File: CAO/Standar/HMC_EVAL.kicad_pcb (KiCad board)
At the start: 2 copper layers, 71 x 83 mm, 57 parts, among them J1 Conn_01x03, J2 Conn_01x03, Q1 IRF7319IPBF, SW1 SW_Push, U1 OPA2209, U2 HMC1001, U4 INA128

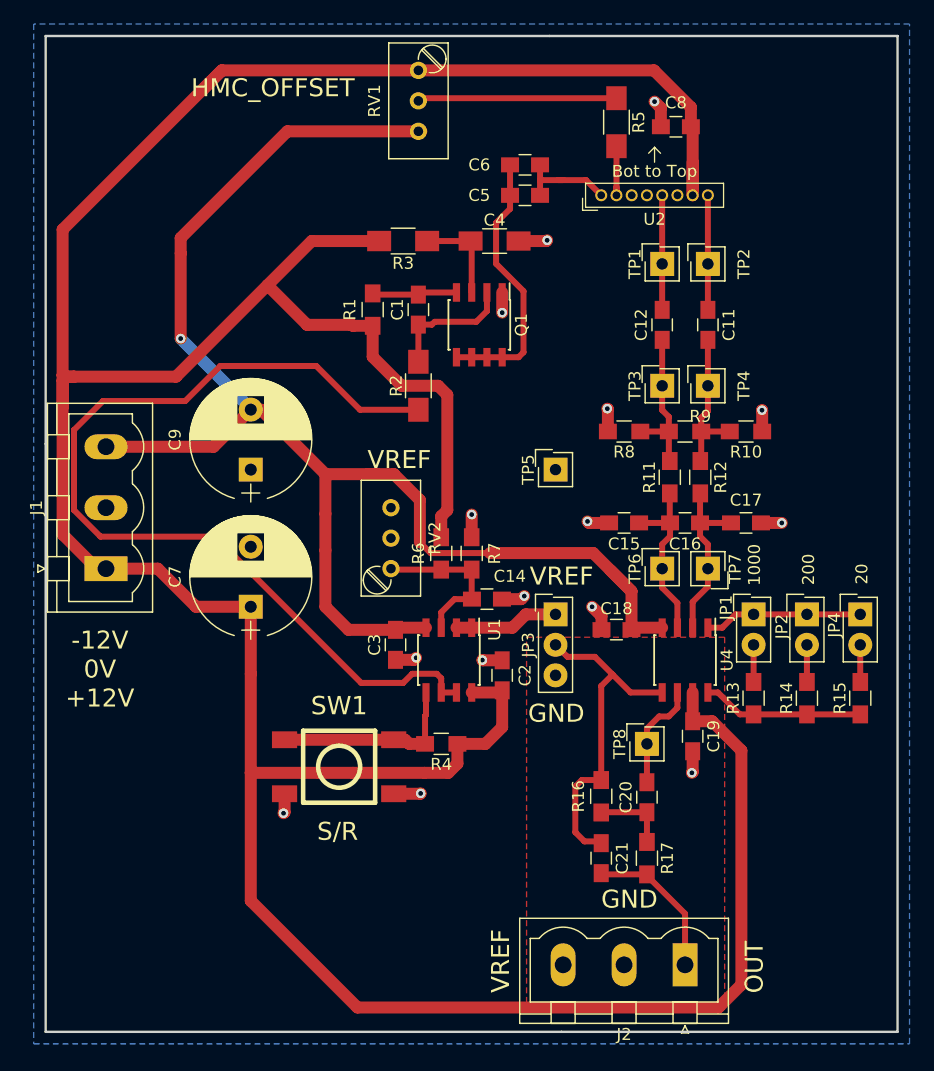
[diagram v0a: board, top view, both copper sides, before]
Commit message: - Low noise version is finish. - Add serigraphi on two design. - Qestion: Copper plane will block low freqency(200hz) magnetic wave??
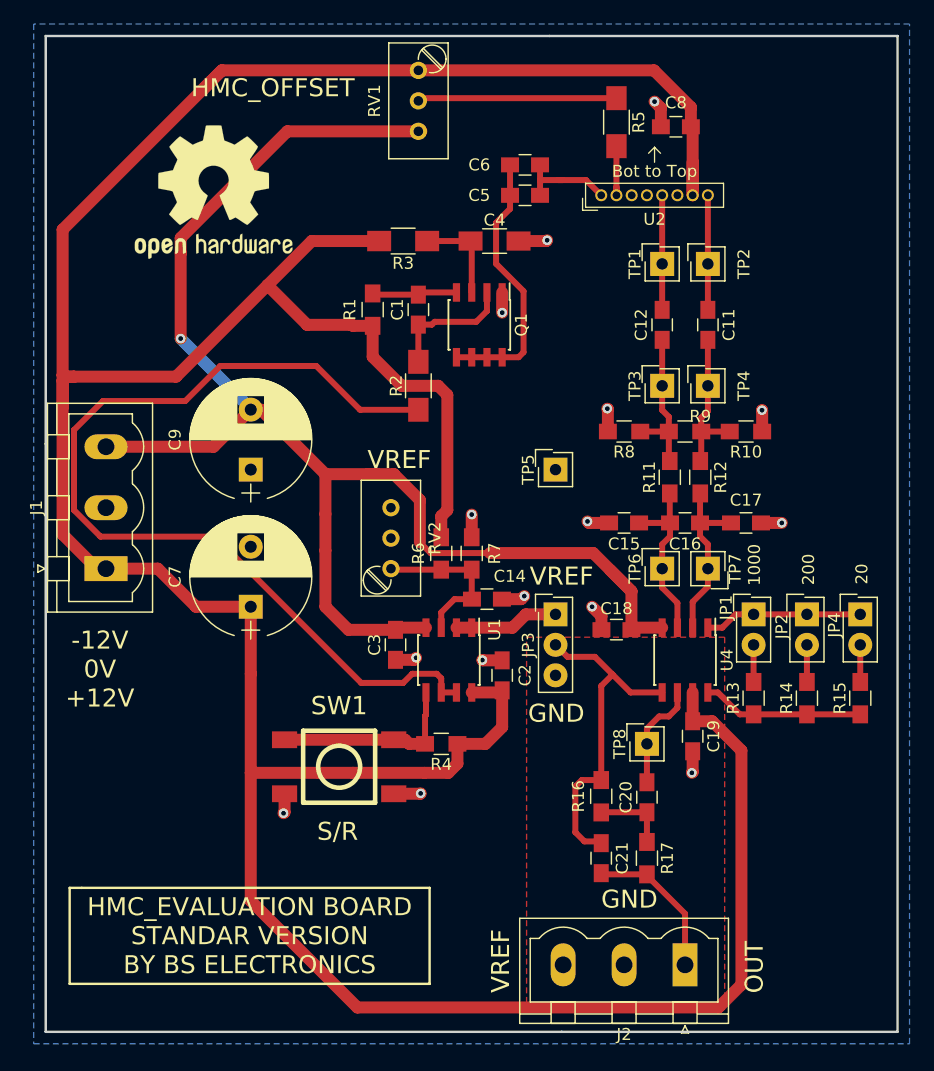
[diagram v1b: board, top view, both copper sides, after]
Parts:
- added REF***: OSHW-Logo2_14.6x12mm_SilkScreen, Symbols:OSHW-Logo2_14.6x12mm_SilkScreen, F.Cu at (96.0, 39.7)
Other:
- board text added: "HMC_EVALUATION BOARD STANDAR VERSION BY BS ELECTRONICS"
